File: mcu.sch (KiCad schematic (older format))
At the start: 18 parts, among them SW19 EVQQ2, SW8 EVQQ2, U9 STM32F405RGTx, Y1 8MHz

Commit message: added package field
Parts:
- C18, C21, C31, C33, C37, C40, C42, C43, R77, R80: Package (none) -> 0603
- C19, C24: Package (none) -> 0805
- U9: Package (none) -> LQFP-64
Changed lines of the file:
@@
 F 4 "STMicroelectronics" H 1600 5225 50  0001 C CNN "MFN"
 F 5 "STM32F405RGT6" H 1600 5225 50  0001 C CNN "MFP"
+F 6 "LQFP-64" H 1600 5225 50  0001 C CNN "Package"
 	1    5800 3200
 	1    0    0    -1
@@
 F 4 "Murata" H 1075 6900 50  0001 C CNN "MFN"
 F 5 "GRM1885C1H180JA01J" H 1075 6900 50  0001 C CNN "MFP"
+F 6 "0603" H 1075 6900 50  0001 C CNN "Package"
 	1    1050 6700
 	0    -1   -1   0
@@
 F 4 "Murata" H 1075 7400 50  0001 C CNN "MFN"
 F 5 "GRM1885C1H180JA01J" H 1075 7400 50  0001 C CNN "MFP"
+F 6 "0603" H 1075 7400 50  0001 C CNN "Package"
 	1    1050 7200
 	0    -1   -1   0
@@
 F 4 "TDK" H 1175 2250 50  0001 C CNN "MFN"
 F 5 "C2012X5R1A225K085AA" H 1175 2250 50  0001 C CNN "MFP"
+F 6 "0805" H 1175 2250 50  0001 C CNN "Package"
 	1    1150 2050
 	0    -1   -1   0
@@
 F 4 "TDK" H 1175 2450 50  0001 C CNN "MFN"
 F 5 "C2012X5R1A225K085AA" H 1175 2450 50  0001 C CNN "MFP"
+F 6 "0805" H 1175 2450 50  0001 C CNN "Package"
 	1    1150 2250
 	0    -1   -1   0
@@
 F 4 "Panasonic" H 5980 6650 50  0001 C CNN "MFN"
 F 5 "ERJ-3EKF1002V" H 5980 6650 50  0001 C CNN "MFP"
+F 6 "0603" H 5980 6650 50  0001 C CNN "Package"
 	1    5900 6550
 	1    0    0    -1
@@
 F 4 "Panasonic" H 6580 7250 50  0001 C CNN "MFN"
 F 5 "ERJ-3EKF1002V" H 6580 7250 50  0001 C CNN "MFP"
+F 6 "0603" H 6580 7250 50  0001 C CNN "Package"
 	1    6500 7150
 	1    0    0    -1
@@
 F 4 "Murata" H 2625 7350 50  0001 C CNN "MFN"
 F 5 "GRM188R71E104JA01J" H 2625 7350 50  0001 C CNN "MFP"
+F 6 "0603" H 2625 7350 50  0001 C CNN "Package"
 	1    2600 7150
 	1    0    0    -1
@@
 F 4 "Murata" H 2925 7350 50  0001 C CNN "MFN"
 F 5 "GRM188R71E104JA01J" H 2925 7350 50  0001 C CNN "MFP"
+F 6 "0603" H 2925 7350 50  0001 C CNN "Package"
 	1    2900 7150
 	1    0    0    -1
@@
 F 4 "Murata" H 3225 7350 50  0001 C CNN "MFN"
 F 5 "GRM188R71E104JA01J" H 3225 7350 50  0001 C CNN "MFP"
+F 6 "0603" H 3225 7350 50  0001 C CNN "Package"
 	1    3200 7150
 	1    0    0    -1
@@
 F 4 "Murata" H 3525 7350 50  0001 C CNN "MFN"
 F 5 "GRM188R71E104JA01J" H 3525 7350 50  0001 C CNN "MFP"
+F 6 "0603" H 3525 7350 50  0001 C CNN "Package"
 	1    3500 7150
 	1    0    0    -1
@@
 F 4 "Murata" H 4025 7350 50  0001 C CNN "MFN"
 F 5 "GRM188R61A105KA61J" H 4025 7350 50  0001 C CNN "MFP"
+F 6 "0603" H 4025 7350 50  0001 C CNN "Package"
 	1    4000 7150
 	1    0    0    -1
@@
 F 4 "Murata" H 4325 7350 50  0001 C CNN "MFN"
 F 5 "GRM188R71E104JA01J" H 4325 7350 50  0001 C CNN "MFP"
+F 6 "0603" H 4325 7350 50  0001 C CNN "Package"
 	1    4300 7150
 	1    0    0    -1

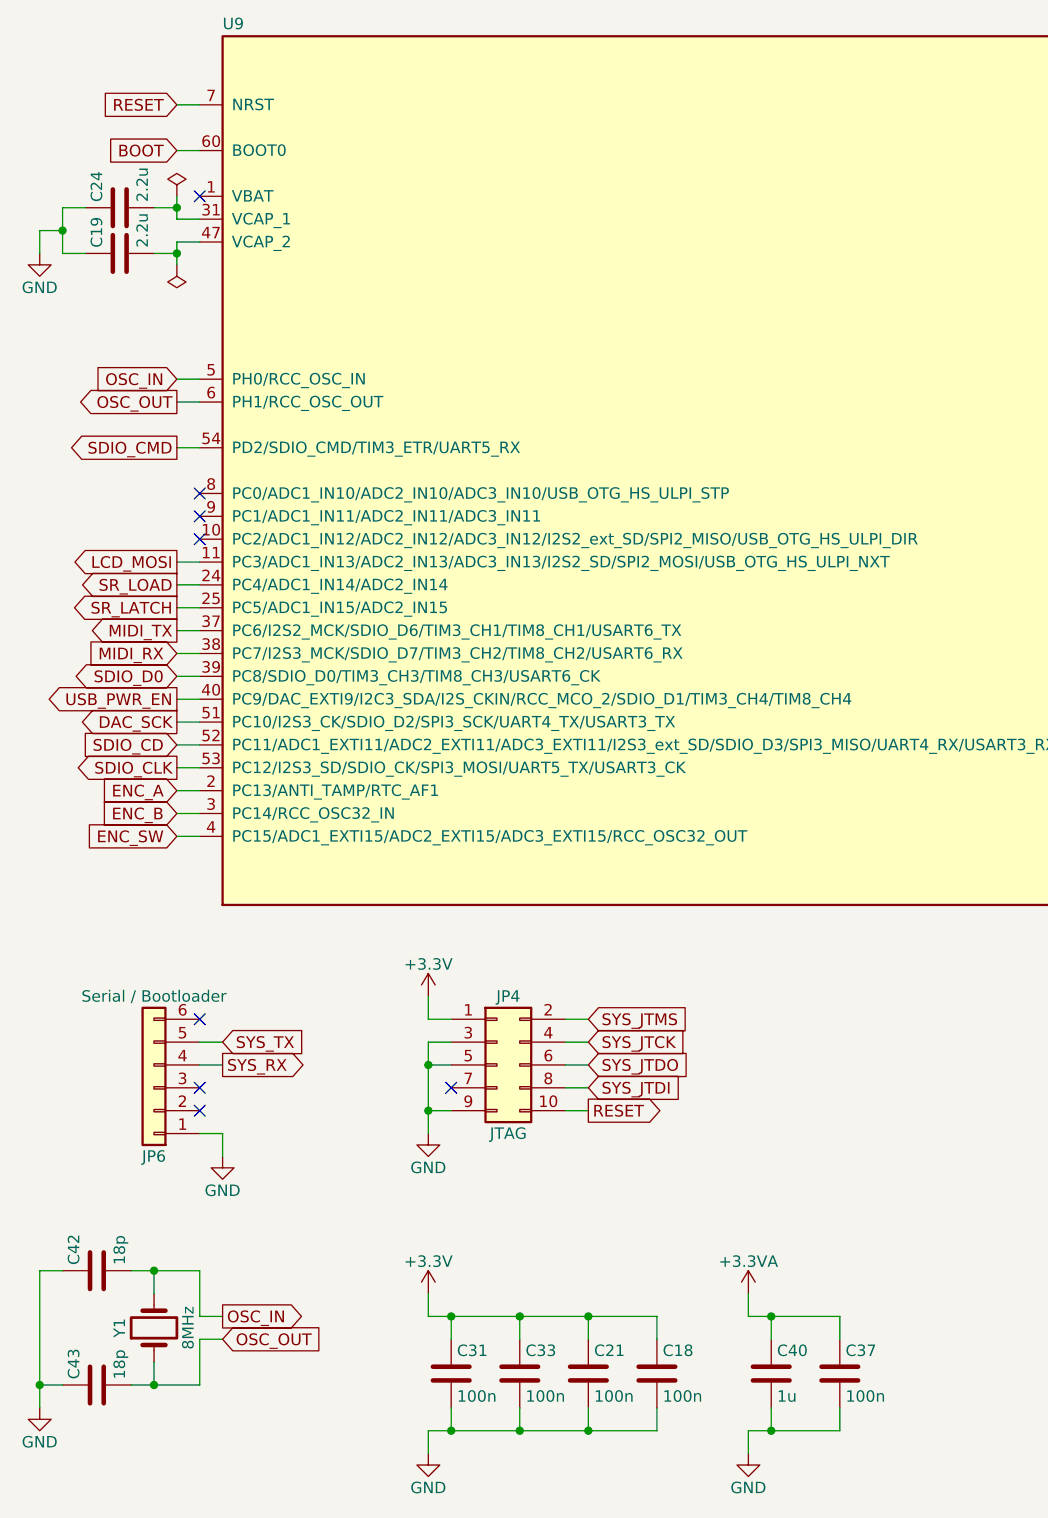
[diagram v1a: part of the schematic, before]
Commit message: renumbered components
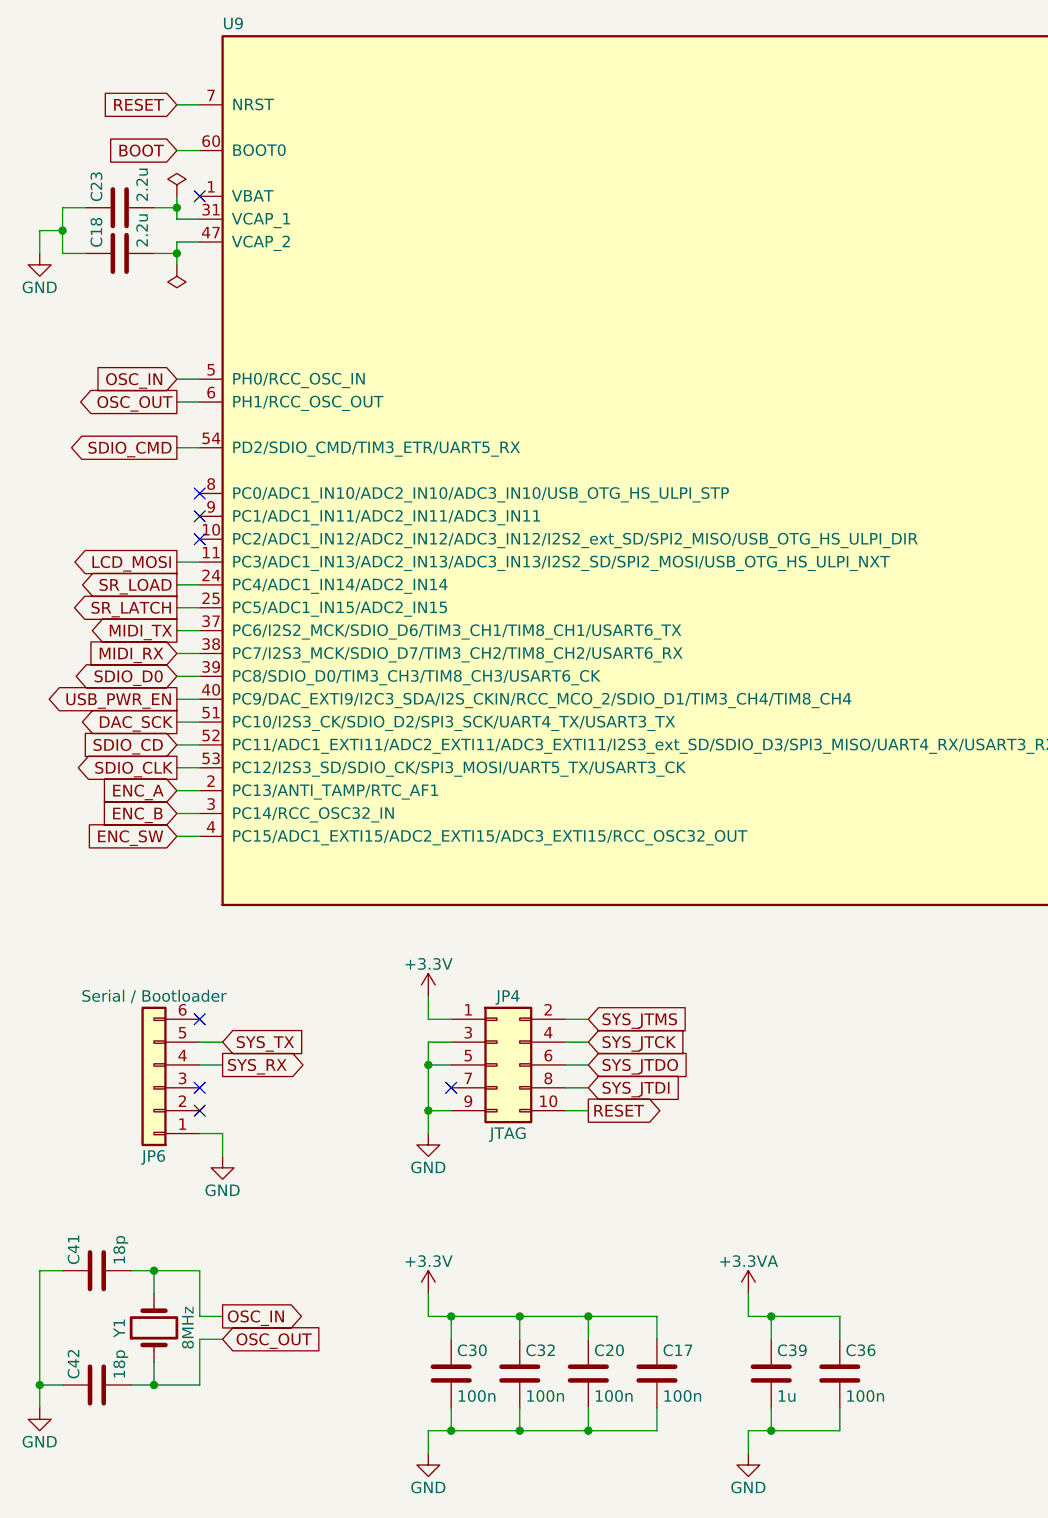
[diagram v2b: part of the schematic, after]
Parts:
- renumbered C18 to C17, C19 to C18, C21 to C20, C24 to C23, C31 to C30, C33 to C32, C37 to C36, C40 to C39, C42 to C41, C43 to C42
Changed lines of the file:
@@
 $EndComp
 $Comp
-L C C42
+L C C41
 U 1 1 59DBA373
 P 1050 6700
-F 0 "C42" H 1075 6800 50  0000 L CNN
+F 0 "C41" H 1075 6800 50  0000 L CNN
 F 1 "18p" H 1075 6600 50  0000 L CNN
 F 2 "w_capacitor:C_0603" H 1088 6550 50  0001 C CNN
@@
 $EndComp
 $Comp
-L C C43
+L C C42
 U 1 1 59DBA3A0
 P 1050 7200
-F 0 "C43" H 1075 7300 50  0000 L CNN
+F 0 "C42" H 1075 7300 50  0000 L CNN
 F 1 "18p" H 1075 7100 50  0000 L CNN
 F 2 "w_capacitor:C_0603" H 1088 7050 50  0001 C CNN
@@
 $EndComp
 $Comp
-L C C24
+L C C23
 U 1 1 59DBB4BE
 P 1150 2050
-F 0 "C24" H 1175 2150 50  0000 L CNN
+F 0 "C23" H 1175 2150 50  0000 L CNN
 F 1 "2.2u" H 1175 1950 50  0000 L CNN
 F 2 "w_capacitor:C_0805" H 1188 1900 50  0001 C CNN
@@
 $EndComp
 $Comp
-L C C19
+L C C18
 U 1 1 59DBB504
 P 1150 2250
-F 0 "C19" H 1175 2350 50  0000 L CNN
+F 0 "C18" H 1175 2350 50  0000 L CNN
 F 1 "2.2u" H 1175 2150 50  0000 L CNN
 F 2 "w_capacitor:C_0805" H 1188 2100 50  0001 C CNN
@@
 $EndComp
 $Comp
-L C C31
+L C C30
 U 1 1 59E34530
 P 2600 7150
-F 0 "C31" H 2625 7250 50  0000 L CNN
+F 0 "C30" H 2625 7250 50  0000 L CNN
 F 1 "100n" H 2625 7050 50  0000 L CNN
 F 2 "w_capacitor:C_0603" H 2638 7000 50  0001 C CNN
@@
 $EndComp
 $Comp
-L C C33
+L C C32
 U 1 1 59E345BC
 P 2900 7150
-F 0 "C33" H 2925 7250 50  0000 L CNN
+F 0 "C32" H 2925 7250 50  0000 L CNN
 F 1 "100n" H 2925 7050 50  0000 L CNN
 F 2 "w_capacitor:C_0603" H 2938 7000 50  0001 C CNN
@@
 $EndComp
 $Comp
-L C C21
+L C C20
 U 1 1 59E34607
 P 3200 7150
-F 0 "C21" H 3225 7250 50  0000 L CNN
+F 0 "C20" H 3225 7250 50  0000 L CNN
 F 1 "100n" H 3225 7050 50  0000 L CNN
 F 2 "w_capacitor:C_0603" H 3238 7000 50  0001 C CNN
@@
 $EndComp
 $Comp
-L C C18
+L C C17
 U 1 1 59E34648
 P 3500 7150
-F 0 "C18" H 3525 7250 50  0000 L CNN
+F 0 "C17" H 3525 7250 50  0000 L CNN
 F 1 "100n" H 3525 7050 50  0000 L CNN
 F 2 "w_capacitor:C_0603" H 3538 7000 50  0001 C CNN
@@
 $EndComp
 $Comp
-L C C40
+L C C39
 U 1 1 59E35219
 P 4000 7150
-F 0 "C40" H 4025 7250 50  0000 L CNN
+F 0 "C39" H 4025 7250 50  0000 L CNN
 F 1 "1u" H 4025 7050 50  0000 L CNN
 F 2 "w_capacitor:C_0603" H 4038 7000 50  0001 C CNN
@@
 $EndComp
 $Comp
-L C C37
+L C C36
 U 1 1 59E3526B
 P 4300 7150
-F 0 "C37" H 4325 7250 50  0000 L CNN
+F 0 "C36" H 4325 7250 50  0000 L CNN
 F 1 "100n" H 4325 7050 50  0000 L CNN
 F 2 "w_capacitor:C_0603" H 4338 7000 50  0001 C CNN

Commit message: cleaned up schematics
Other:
- note added: "Connects to standard\nFTDI 3.3V serial adapter"
- note added: "JTAG PORT"
- note added: "RESET / BOOT BUTTONS"
- note added: "SERIAL PORT"
- note added: "STM32"
- moved on the sheet: C17, C20, C30, C32, C36, C39, C41, C42, JP4, JP6, R77, R80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

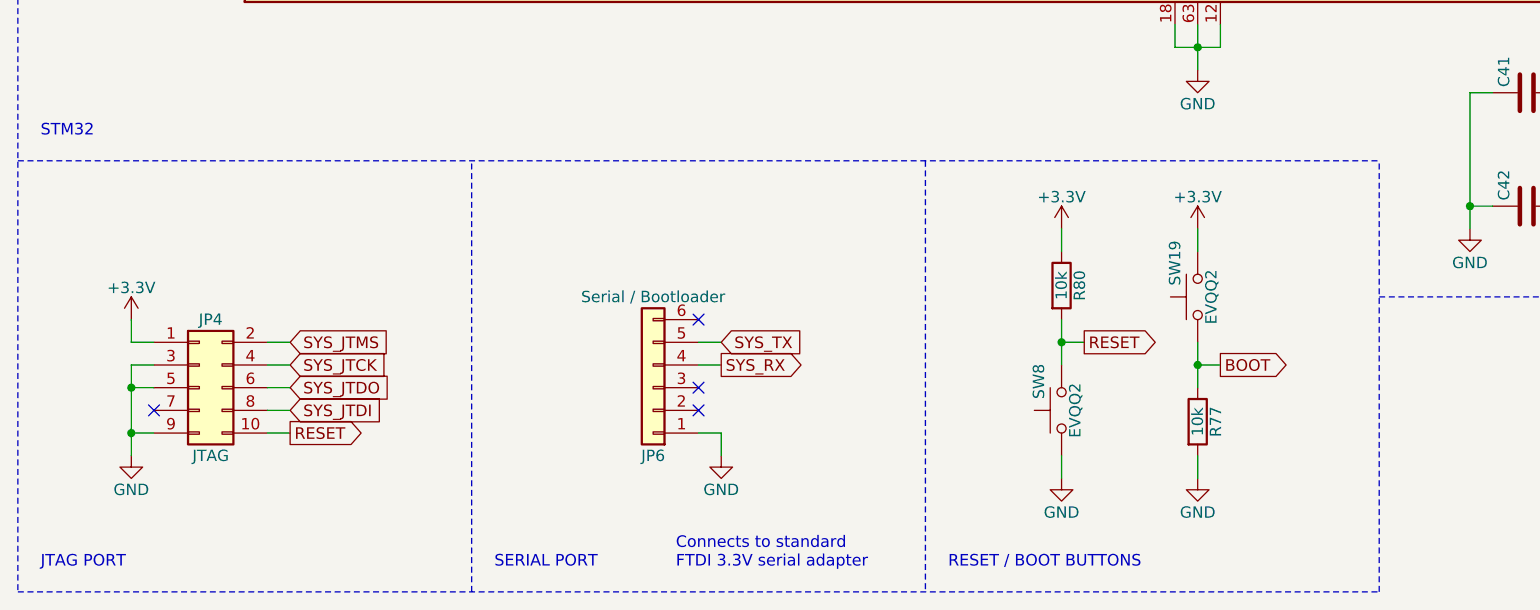
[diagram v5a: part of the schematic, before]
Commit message: revised schematic and pcb
- fixed clock/reset inputs
- schematic annotations
- moved to cc-by-nc-sa
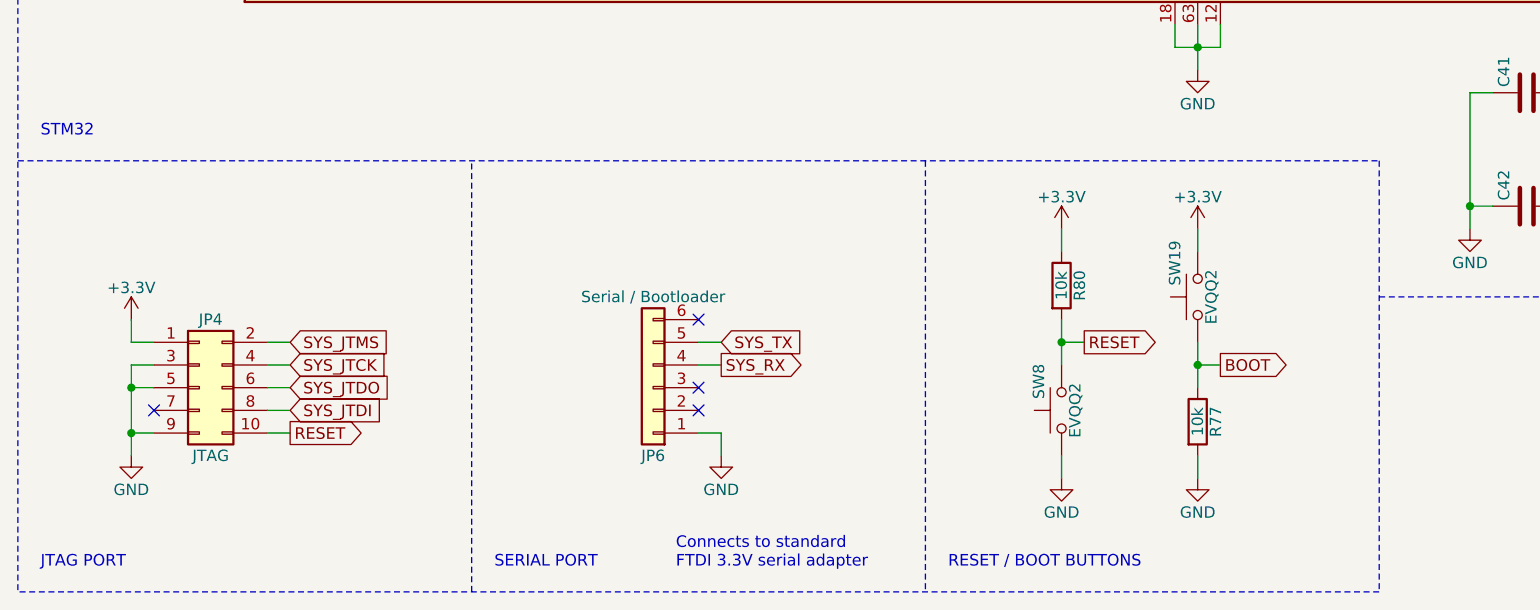
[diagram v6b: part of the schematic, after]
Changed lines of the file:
@@
 Text GLabel 10200 2000 2    51   Output ~ 0
 SR_OE
+Text Notes 700  5700 0    51   ~ 0
+STM32
+Text Notes 4700 7600 0    51   ~ 0
+RESET / BOOT BUTTONS
+Text Notes 2700 7600 0    51   ~ 0
+SERIAL PORT
+Text Notes 700  7600 0    51   ~ 0
+JTAG PORT
+Text Notes 3500 7600 0    51   ~ 0
+Connects to standard\nFTDI 3.3V serial adapter
 Wire Wire Line
 	3600 7000 3700 7000
@@
 Wire Wire Line
 	10100 2000 10200 2000
+Wire Notes Line
+	600  600  600  7700
+Wire Notes Line
+	600  5800 6600 5800
+Wire Notes Line
+	6600 5800 6600 7700
+Wire Notes Line
+	6600 6400 11100 6400
+Wire Notes Line
+	11100 6400 11100 600
+Wire Notes Line
+	11100 600  600  600
+Wire Notes Line
+	4600 5800 4600 7700
+Wire Notes Line
+	6600 7700 600  7700
+Wire Notes Line
+	2600 7700 2600 5800
 Connection ~ 1100 7000
 Connection ~ 1100 6800
@@
 NoConn ~ 1500 3300
 NoConn ~ 1500 3400
-Wire Notes Line
-	600  600  600  7700
-Wire Notes Line
-	600  5800 6600 5800
-Wire Notes Line
-	6600 7700 6600 5800
-Wire Notes Line
-	6600 6400 11100 6400
-Wire Notes Line
-	11100 6400 11100 600
-Wire Notes Line
-	11100 600  600  600
-Text Notes 700  5700 0    51   ~ 0
-STM32
-Wire Notes Line
-	4600 5800 4600 7700
-Wire Notes Line
-	600  7700 6600 7700
-Text Notes 4700 7600 0    51   ~ 0
-RESET / BOOT BUTTONS
-Wire Notes Line
-	2600 7700 2600 5800
-Text Notes 2700 7600 0    51   ~ 0
-SERIAL PORT
-Text Notes 700  7600 0    51   ~ 0
-JTAG PORT
-Text Notes 3500 7600 0    51   ~ 0
-Connects to standard\nFTDI 3.3V serial adapter
 $EndSCHEMATC

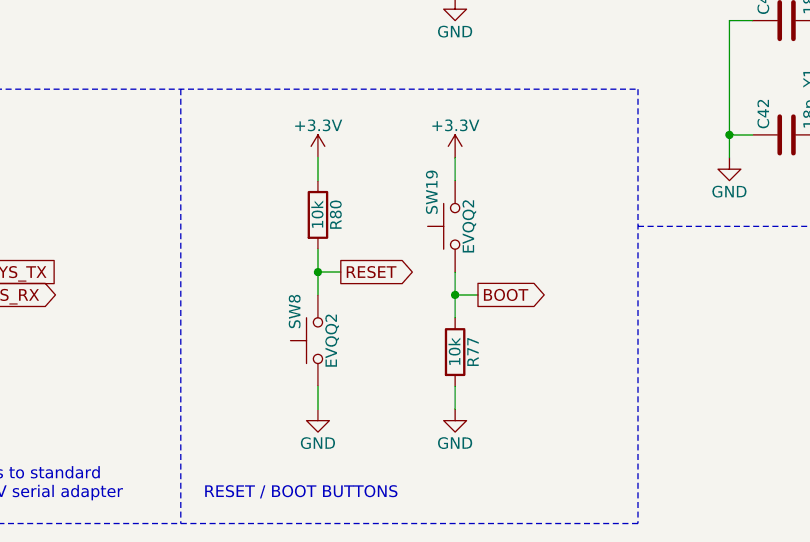
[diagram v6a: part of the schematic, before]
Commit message: renumbered components
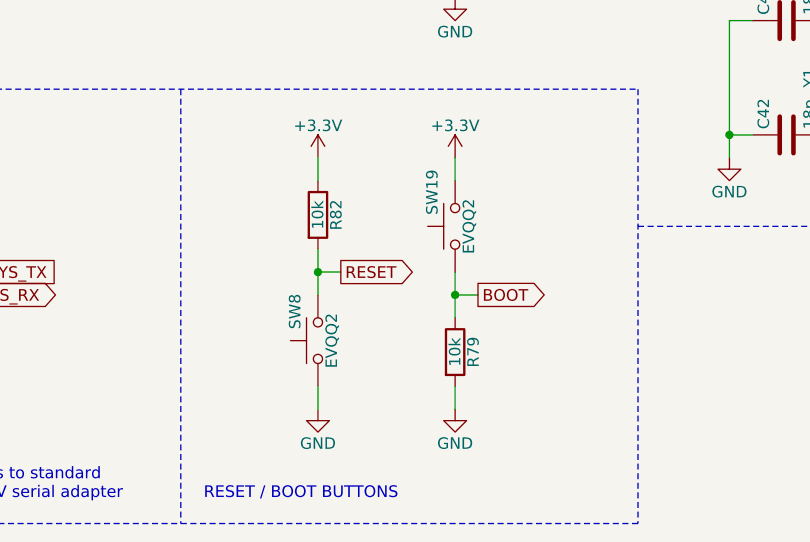
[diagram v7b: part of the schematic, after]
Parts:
- renumbered R77 to R79, R80 to R82
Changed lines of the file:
@@
 $EndComp
 $Comp
-L R R80
+L R R82
 U 1 1 59DD490D
 P 5200 6350
-F 0 "R80" V 5280 6350 50  0000 C CNN
+F 0 "R82" V 5280 6350 50  0000 C CNN
 F 1 "10k" V 5200 6350 50  0000 C CNN
 F 2 "w_resistor:R_0603" V 5130 6350 50  0001 C CNN
@@
 $EndComp
 $Comp
-L R R77
+L R R79
 U 1 1 59DD4953
 P 5800 6950
-F 0 "R77" V 5880 6950 50  0000 C CNN
+F 0 "R79" V 5880 6950 50  0000 C CNN
 F 1 "10k" V 5800 6950 50  0000 C CNN
 F 2 "w_resistor:R_0603" V 5730 6950 50  0001 C CNN
